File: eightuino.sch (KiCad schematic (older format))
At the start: 21 parts, among them CON1 BARREL_JACK, CON2 AVR-ISP-10, IC1 ATMEGA8-P, P1 PowerPins, P2 Analog, P3 Digital1, P4 Digital_2, SW1 SW_PUSH_SMALL, U1 NCP1117ST33T3G, X1 CRYSTAL

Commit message: Added FTDI connector in schematic
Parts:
- added C?: 100nF, symbol C
- added P?: CONN_6, symbol CONN_6
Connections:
- net +BATT: now also P?.3
- net GND: now also P?.1, P?.2
- net at CON2.5, IC1.1 (PC6(~RESET~)), P1.6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: now also C?.2
- net RX: now reaches IC1.2 ((RXD)PD0), P3.1 (P1)
- net RX: now also P?.4
- net TX: now reaches IC1.3 ((TXD)PD1), P3.2 (P2)
- net TX: now also P?.5
- new net DTR: C?.1, P?.6

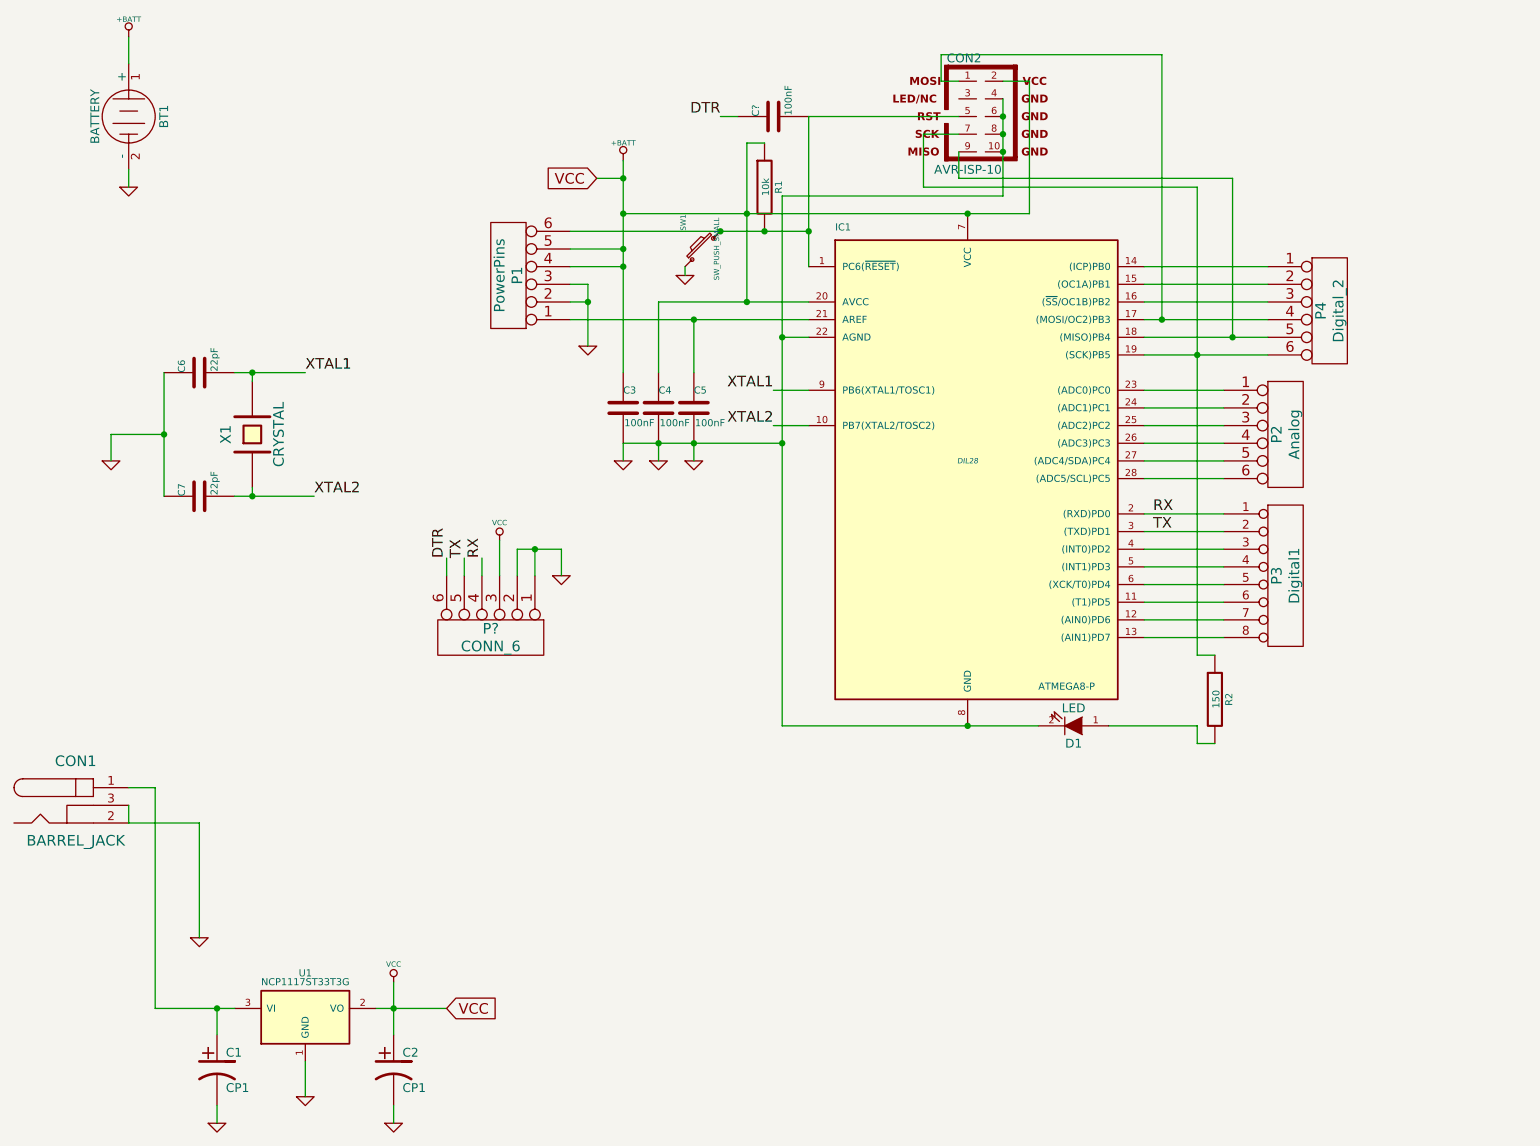
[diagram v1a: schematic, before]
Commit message: Changed schematic to 6-pin ISP
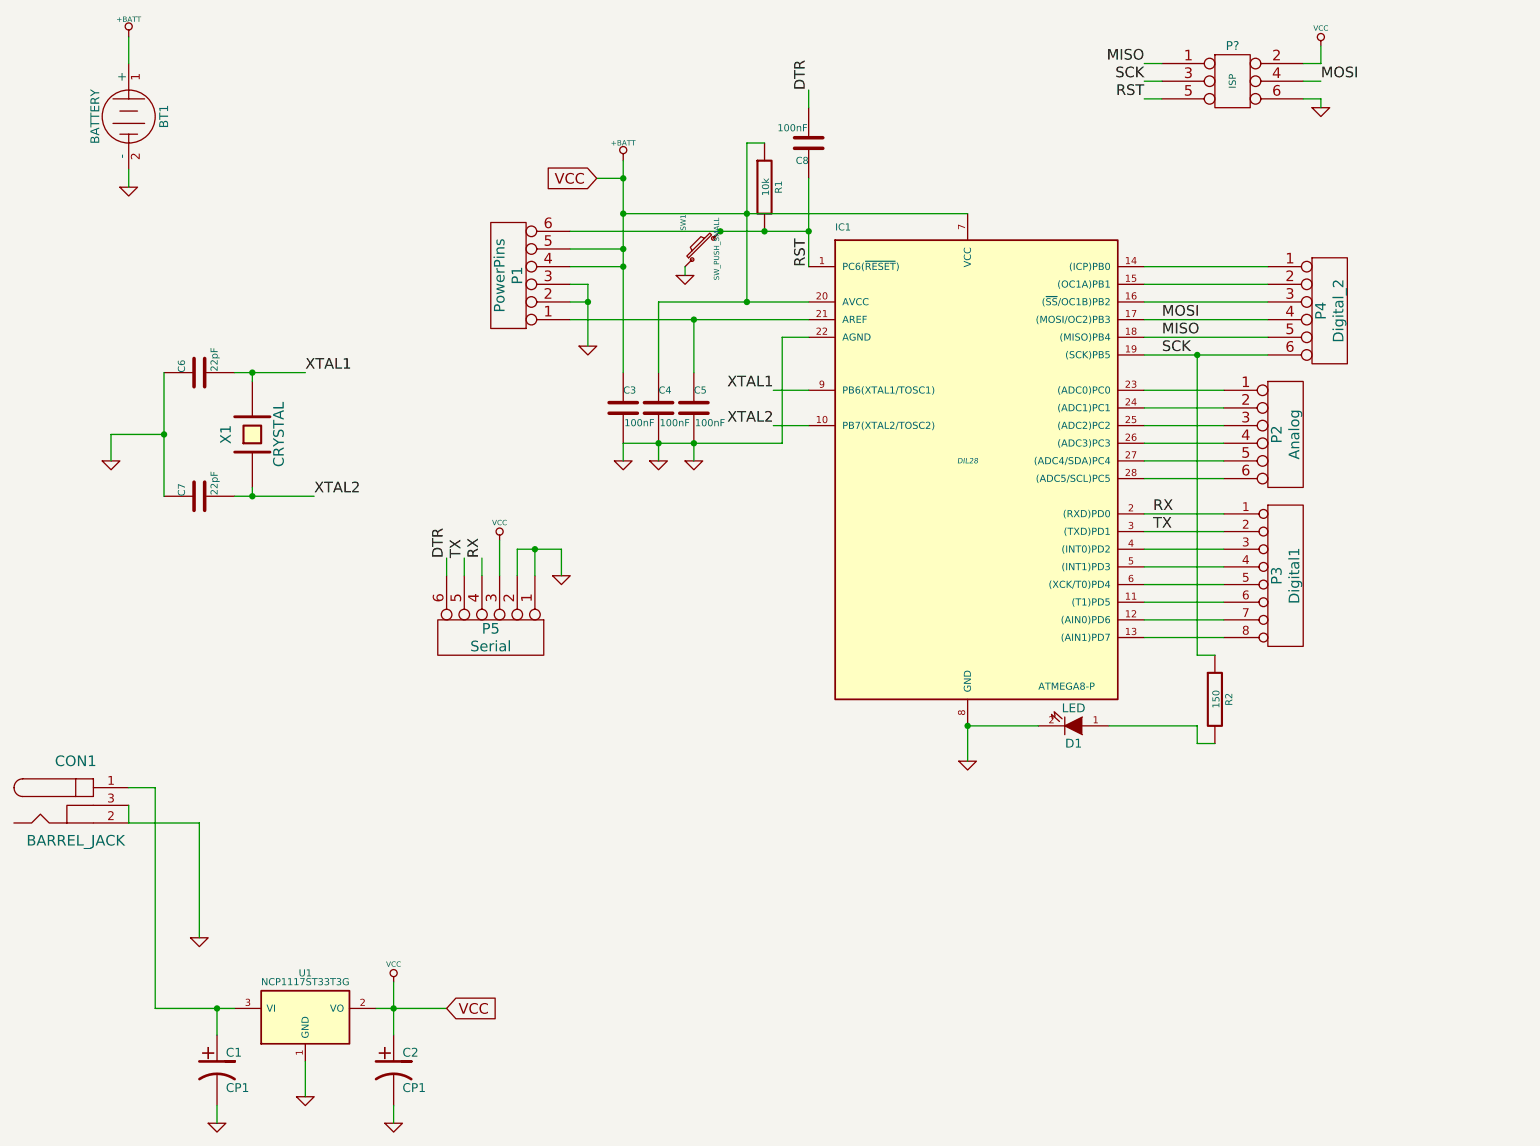
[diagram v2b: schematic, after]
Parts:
- removed CON2: AVR-ISP-10, AVR-ISP-10, symbol AVR-ISP-10
- added P?: ISP, symbol CONN_3X2
- P5: renamed from P?; value CONN_6 -> Serial
- gave numbers to parts that had none: 1
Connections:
- net +BATT: now also P?.2
- net DTR: now also C8.2; no longer C8.1
- net GND: now also P?.6
- net RST: now reaches IC1.1 (PC6(~RESET~)), P1.6, R1.2, SW1.2
- net RST: now also C8.1, P?.5; no longer C8.2
- net MOSI: now reaches IC1.17 ((MOSI/OC2)PB3), P4.4
- net MOSI: now also P?.4
- net MISO: now reaches IC1.18 ((MISO)PB4), P4.5
- net MISO: now also P?.1
- net SCK: now reaches IC1.19 ((SCK)PB5), P4.6, R2.1
- net SCK: now also P?.3
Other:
- moved on the sheet: C8

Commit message: Almost total board rework.
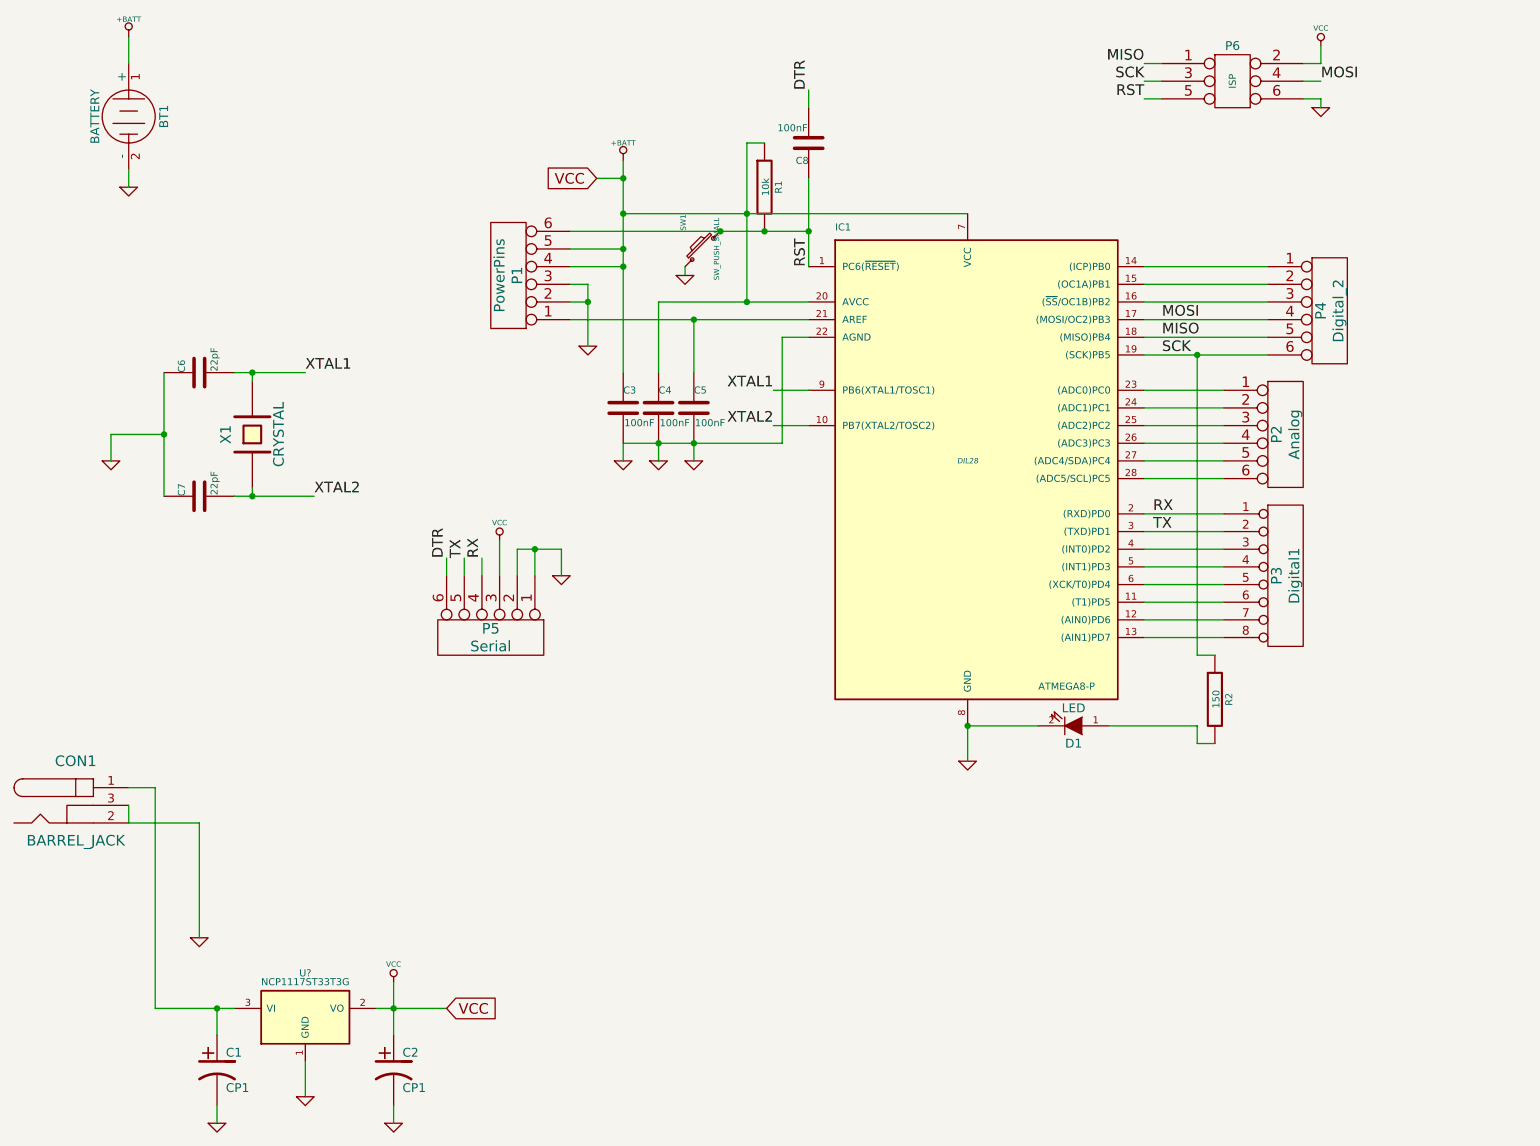
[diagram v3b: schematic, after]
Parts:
- removed U1: NCP1117ST33T3G, ~, symbol NCP1117ST33T3G
- added U?: NCP1117ST33T3G, symbol NCP1117ST33T3G
- gave numbers to parts that had none: 1
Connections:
- net +BATT: now also U?.2 (VO)
- net GND: now also U?.1 (GND)
- net at C1.1, CON1.1: now also U?.3 (VI)
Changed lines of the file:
@@
 $EndComp
 $Comp
-L GND #PWR16
+L GND #PWR01
 U 1 1 528D0B5A
 P 5300 3300
-F 0 "#PWR16" H 5300 3300 30  0001 C CNN
+F 0 "#PWR01" H 5300 3300 30  0001 C CNN
 F 1 "GND" H 5300 3230 30  0001 C CNN
 F 2 "" H 5300 3300 60  0000 C CNN
@@
 $EndComp
 $Comp
-L GND #PWR14
+L GND #PWR02
 U 1 1 528D0B67
 P 5100 3300
-F 0 "#PWR14" H 5100 3300 30  0001 C CNN
+F 0 "#PWR02" H 5100 3300 30  0001 C CNN
 F 1 "GND" H 5100 3230 30  0001 C CNN
 F 2 "" H 5100 3300 60  0000 C CNN
@@
 $EndComp
 $Comp
-L GND #PWR13
+L GND #PWR03
 U 1 1 528D0B6D
 P 4900 3300
-F 0 "#PWR13" H 4900 3300 30  0001 C CNN
+F 0 "#PWR03" H 4900 3300 30  0001 C CNN
 F 1 "GND" H 4900 3230 30  0001 C CNN
 F 2 "" H 4900 3300 60  0000 C CNN
@@
 $EndComp
 $Comp
-L GND #PWR11
+L GND #PWR04
 U 1 1 528D0D22
 P 4700 2650
-F 0 "#PWR11" H 4700 2650 30  0001 C CNN
+F 0 "#PWR04" H 4700 2650 30  0001 C CNN
 F 1 "GND" H 4700 2580 30  0001 C CNN
 F 2 "" H 4700 2650 60  0000 C CNN
@@
 $EndComp
 $Comp
-L GND #PWR15
+L GND #PWR05
 U 1 1 528D1116
 P 5250 2250
-F 0 "#PWR15" H 5250 2250 30  0001 C CNN
+F 0 "#PWR05" H 5250 2250 30  0001 C CNN
 F 1 "GND" H 5250 2180 30  0001 C CNN
 F 2 "" H 5250 2250 60  0000 C CNN
@@
 $EndComp
 $Comp
-L NCP1117ST33T3G U1
-U 1 1 5293AD98
-P 3100 6450
-F 0 "U1" H 3100 6700 40  0000 C CNN
-F 1 "NCP1117ST33T3G" H 3100 6650 40  0000 C CNN
-F 2 "~" H 3100 6450 60  0000 C CNN
-F 3 "~" H 3100 6450 60  0000 C CNN
-	1    3100 6450
-	1    0    0    -1
-$EndComp
-$Comp
-L GND #PWR4
+L GND #PWR06
 U 1 1 5293AE0F
 P 2500 6000
-F 0 "#PWR4" H 2500 6000 30  0001 C CNN
+F 0 "#PWR06" H 2500 6000 30  0001 C CNN
 F 1 "GND" H 2500 5930 30  0001 C CNN
 F 2 "" H 2500 6000 60  0000 C CNN
@@
 $EndComp
 $Comp
-L GND #PWR6
+L GND #PWR07
 U 1 1 5293AEC4
 P 3100 6900
-F 0 "#PWR6" H 3100 6900 30  0001 C CNN
+F 0 "#PWR07" H 3100 6900 30  0001 C CNN
 F 1 "GND" H 3100 6830 30  0001 C CNN
 F 2 "" H 3100 6900 60  0000 C CNN
@@
 $EndComp
 $Comp
-L GND #PWR5
+L GND #PWR08
 U 1 1 5293AF43
 P 2600 7050
-F 0 "#PWR5" H 2600 7050 30  0001 C CNN
+F 0 "#PWR08" H 2600 7050 30  0001 C CNN
 F 1 "GND" H 2600 6980 30  0001 C CNN
 F 2 "" H 2600 7050 60  0000 C CNN
@@
 $EndComp
 $Comp
-L GND #PWR8
+L GND #PWR09
 U 1 1 5293AF49
 P 3600 7050
-F 0 "#PWR8" H 3600 7050 30  0001 C CNN
+F 0 "#PWR09" H 3600 7050 30  0001 C CNN
 F 1 "GND" H 3600 6980 30  0001 C CNN
 F 2 "" H 3600 7050 60  0000 C CNN
@@
 $EndComp
 $Comp
-L GND #PWR3
+L GND #PWR010
 U 1 1 52B96E7A
 P 2100 1750
-F 0 "#PWR3" H 2100 1750 30  0001 C CNN
+F 0 "#PWR010" H 2100 1750 30  0001 C CNN
 F 1 "GND" H 2100 1680 30  0001 C CNN
 F 2 "" H 2100 1750 60  0000 C CNN
@@
 $EndComp
 $Comp
-L +BATT #PWR2
+L +BATT #PWR011
 U 1 1 52B97066
 P 2100 900
-F 0 "#PWR2" H 2100 850 20  0001 C CNN
+F 0 "#PWR011" H 2100 850 20  0001 C CNN
 F 1 "+BATT" H 2100 1000 30  0000 C CNN
 F 2 "" H 2100 900 60  0000 C CNN
@@
 $EndComp
 $Comp
-L +BATT #PWR12
+L +BATT #PWR012
 U 1 1 52B9707A
 P 4900 1600
-F 0 "#PWR12" H 4900 1550 20  0001 C CNN
+F 0 "#PWR012" H 4900 1550 20  0001 C CNN
 F 1 "+BATT" H 4900 1700 30  0000 C CNN
 F 2 "" H 4900 1600 60  0000 C CNN
@@
 $EndComp
 $Comp
-L GND #PWR1
+L GND #PWR013
 U 1 1 52B97A43
 P 2000 3300
-F 0 "#PWR1" H 2000 3300 30  0001 C CNN
+F 0 "#PWR013" H 2000 3300 30  0001 C CNN
 F 1 "GND" H 2000 3230 30  0001 C CNN
 F 2 "" H 2000 3300 60  0000 C CNN
@@
 $EndComp
 $Comp
-L GND #PWR10
+L GND #PWR014
 U 1 1 52D5A868
 P 4550 3950
-F 0 "#PWR10" H 4550 3950 30  0001 C CNN
+F 0 "#PWR014" H 4550 3950 30  0001 C CNN
 F 1 "GND" H 4550 3880 30  0001 C CNN
 F 2 "" H 4550 3950 60  0000 C CNN
@@
 $EndComp
 $Comp
-L VCC #PWR7
+L VCC #PWR015
 U 1 1 52D5AB5A
 P 3600 6250
-F 0 "#PWR7" H 3600 6350 30  0001 C CNN
+F 0 "#PWR015" H 3600 6350 30  0001 C CNN
 F 1 "VCC" H 3600 6350 30  0000 C CNN
 F 2 "" H 3600 6250 60  0000 C CNN
@@
 $EndComp
 $Comp
-L VCC #PWR9
+L VCC #PWR016
 U 1 1 52D5ACF4
 P 4200 3750
-F 0 "#PWR9" H 4200 3850 30  0001 C CNN
+F 0 "#PWR016" H 4200 3850 30  0001 C CNN
 F 1 "VCC" H 4200 3850 30  0000 C CNN
 F 2 "" H 4200 3750 60  0000 C CNN
@@
 TX
 $Comp
-L CONN_3X2 P?
+L CONN_3X2 P6
 U 1 1 52D6FAC9
 P 8350 1200
-F 0 "P?" H 8350 1450 50  0000 C CNN
+F 0 "P6" H 8350 1450 50  0000 C CNN
 F 1 "ISP" V 8350 1250 40  0000 C CNN
 F 2 "" H 8350 1200 60  0000 C CNN
@@
 MOSI
 $Comp
-L VCC #PWR?
+L VCC #PWR017
 U 1 1 52D6FB73
 P 8850 950
-F 0 "#PWR?" H 8850 1050 30  0001 C CNN
+F 0 "#PWR017" H 8850 1050 30  0001 C CNN
 F 1 "VCC" H 8850 1050 30  0000 C CNN
 F 2 "" H 8850 950 60  0000 C CNN
@@
 $EndComp
 $Comp
-L GND #PWR?
+L GND #PWR018
 U 1 1 52D6FC04
 P 8850 1300
-F 0 "#PWR?" H 8850 1300 30  0001 C CNN
+F 0 "#PWR018" H 8850 1300 30  0001 C CNN
 F 1 "GND" H 8850 1230 30  0001 C CNN
 F 2 "" H 8850 1300 60  0000 C CNN
@@
 RST
 $Comp
-L GND #PWR?
+L GND #PWR019
 U 1 1 52D7024C
 P 6850 5000
-F 0 "#PWR?" H 6850 5000 30  0001 C CNN
+F 0 "#PWR019" H 6850 5000 30  0001 C CNN
 F 1 "GND" H 6850 4930 30  0001 C CNN
 F 2 "" H 6850 5000 60  0000 C CNN
@@
 	3600 6250 3600 6550
 Wire Wire Line
-	2250 6400 2700 6400
-Wire Wire Line
 	2600 6550 2600 6400
 Wire Wire Line
@@
 Wire Wire Line
 	4900 1900 6850 1900
+Wire Wire Line
+	2250 6400 2700 6400
+$Comp
+L NCP1117ST33T3G U?
+U 1 1 52D7F944
+P 3100 6450
+F 0 "U?" H 3100 6700 40  0000 C CNN
+F 1 "NCP1117ST33T3G" H 3100 6650 40  0000 C CNN
+F 2 "" H 3100 6450 60  0000 C CNN
+F 3 "" H 3100 6450 60  0000 C CNN
+	1    3100 6450
+	1    0    0    -1
+$EndComp
 $EndSCHEMATC

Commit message: Remembered to save schematic
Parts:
- gave numbers to parts that had none: 1
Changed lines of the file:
@@
 $EndComp
 $Comp
-L GND #PWR01
+L GND #PWR16
 U 1 1 528D0B5A
 P 5300 3300
-F 0 "#PWR01" H 5300 3300 30  0001 C CNN
+F 0 "#PWR16" H 5300 3300 30  0001 C CNN
 F 1 "GND" H 5300 3230 30  0001 C CNN
 F 2 "" H 5300 3300 60  0000 C CNN
@@
 $EndComp
 $Comp
-L GND #PWR02
+L GND #PWR14
 U 1 1 528D0B67
 P 5100 3300
-F 0 "#PWR02" H 5100 3300 30  0001 C CNN
+F 0 "#PWR14" H 5100 3300 30  0001 C CNN
 F 1 "GND" H 5100 3230 30  0001 C CNN
 F 2 "" H 5100 3300 60  0000 C CNN
@@
 $EndComp
 $Comp
-L GND #PWR03
+L GND #PWR13
 U 1 1 528D0B6D
 P 4900 3300
-F 0 "#PWR03" H 4900 3300 30  0001 C CNN
+F 0 "#PWR13" H 4900 3300 30  0001 C CNN
 F 1 "GND" H 4900 3230 30  0001 C CNN
 F 2 "" H 4900 3300 60  0000 C CNN
@@
 $EndComp
 $Comp
-L GND #PWR04
+L GND #PWR11
 U 1 1 528D0D22
 P 4700 2650
-F 0 "#PWR04" H 4700 2650 30  0001 C CNN
+F 0 "#PWR11" H 4700 2650 30  0001 C CNN
 F 1 "GND" H 4700 2580 30  0001 C CNN
 F 2 "" H 4700 2650 60  0000 C CNN
@@
 $EndComp
 $Comp
-L GND #PWR05
+L GND #PWR15
 U 1 1 528D1116
 P 5250 2250
-F 0 "#PWR05" H 5250 2250 30  0001 C CNN
+F 0 "#PWR15" H 5250 2250 30  0001 C CNN
 F 1 "GND" H 5250 2180 30  0001 C CNN
 F 2 "" H 5250 2250 60  0000 C CNN
@@
 $EndComp
 $Comp
-L GND #PWR06
+L GND #PWR4
 U 1 1 5293AE0F
 P 2500 6000
-F 0 "#PWR06" H 2500 6000 30  0001 C CNN
+F 0 "#PWR4" H 2500 6000 30  0001 C CNN
 F 1 "GND" H 2500 5930 30  0001 C CNN
 F 2 "" H 2500 6000 60  0000 C CNN
@@
 $EndComp
 $Comp
-L GND #PWR07
+L GND #PWR6
 U 1 1 5293AEC4
 P 3100 6900
-F 0 "#PWR07" H 3100 6900 30  0001 C CNN
+F 0 "#PWR6" H 3100 6900 30  0001 C CNN
 F 1 "GND" H 3100 6830 30  0001 C CNN
 F 2 "" H 3100 6900 60  0000 C CNN
@@
 $EndComp
 $Comp
-L GND #PWR08
+L GND #PWR5
 U 1 1 5293AF43
 P 2600 7050
-F 0 "#PWR08" H 2600 7050 30  0001 C CNN
+F 0 "#PWR5" H 2600 7050 30  0001 C CNN
 F 1 "GND" H 2600 6980 30  0001 C CNN
 F 2 "" H 2600 7050 60  0000 C CNN
@@
 $EndComp
 $Comp
-L GND #PWR09
+L GND #PWR8
 U 1 1 5293AF49
 P 3600 7050
-F 0 "#PWR09" H 3600 7050 30  0001 C CNN
+F 0 "#PWR8" H 3600 7050 30  0001 C CNN
 F 1 "GND" H 3600 6980 30  0001 C CNN
 F 2 "" H 3600 7050 60  0000 C CNN
@@
 $EndComp
 $Comp
-L GND #PWR010
+L GND #PWR3
 U 1 1 52B96E7A
 P 2100 1750
-F 0 "#PWR010" H 2100 1750 30  0001 C CNN
+F 0 "#PWR3" H 2100 1750 30  0001 C CNN
 F 1 "GND" H 2100 1680 30  0001 C CNN
 F 2 "" H 2100 1750 60  0000 C CNN
@@
 $EndComp
 $Comp
-L +BATT #PWR011
+L +BATT #PWR2
 U 1 1 52B97066
 P 2100 900
-F 0 "#PWR011" H 2100 850 20  0001 C CNN
+F 0 "#PWR2" H 2100 850 20  0001 C CNN
 F 1 "+BATT" H 2100 1000 30  0000 C CNN
 F 2 "" H 2100 900 60  0000 C CNN
@@
 $EndComp
 $Comp
-L +BATT #PWR012
+L +BATT #PWR12
 U 1 1 52B9707A
 P 4900 1600
-F 0 "#PWR012" H 4900 1550 20  0001 C CNN
+F 0 "#PWR12" H 4900 1550 20  0001 C CNN
 F 1 "+BATT" H 4900 1700 30  0000 C CNN
 F 2 "" H 4900 1600 60  0000 C CNN
@@
 $EndComp
 $Comp
-L GND #PWR013
+L GND #PWR1
 U 1 1 52B97A43
 P 2000 3300
-F 0 "#PWR013" H 2000 3300 30  0001 C CNN
+F 0 "#PWR1" H 2000 3300 30  0001 C CNN
 F 1 "GND" H 2000 3230 30  0001 C CNN
 F 2 "" H 2000 3300 60  0000 C CNN
@@
 $EndComp
 $Comp
-L GND #PWR014
+L GND #PWR10
 U 1 1 52D5A868
 P 4550 3950
-F 0 "#PWR014" H 4550 3950 30  0001 C CNN
+F 0 "#PWR10" H 4550 3950 30  0001 C CNN
 F 1 "GND" H 4550 3880 30  0001 C CNN
 F 2 "" H 4550 3950 60  0000 C CNN
@@
 $EndComp
 $Comp
-L VCC #PWR015
+L VCC #PWR7
 U 1 1 52D5AB5A
 P 3600 6250
-F 0 "#PWR015" H 3600 6350 30  0001 C CNN
+F 0 "#PWR7" H 3600 6350 30  0001 C CNN
 F 1 "VCC" H 3600 6350 30  0000 C CNN
 F 2 "" H 3600 6250 60  0000 C CNN
@@
 $EndComp
 $Comp
-L VCC #PWR016
+L VCC #PWR9
 U 1 1 52D5ACF4
 P 4200 3750
-F 0 "#PWR016" H 4200 3850 30  0001 C CNN
+F 0 "#PWR9" H 4200 3850 30  0001 C CNN
 F 1 "VCC" H 4200 3850 30  0000 C CNN
 F 2 "" H 4200 3750 60  0000 C CNN
@@
 MOSI
 $Comp
-L VCC #PWR017
+L VCC #PWR18
 U 1 1 52D6FB73
 P 8850 950
-F 0 "#PWR017" H 8850 1050 30  0001 C CNN
+F 0 "#PWR18" H 8850 1050 30  0001 C CNN
 F 1 "VCC" H 8850 1050 30  0000 C CNN
 F 2 "" H 8850 950 60  0000 C CNN
@@
 $EndComp
 $Comp
-L GND #PWR018
+L GND #PWR19
 U 1 1 52D6FC04
 P 8850 1300
-F 0 "#PWR018" H 8850 1300 30  0001 C CNN
+F 0 "#PWR19" H 8850 1300 30  0001 C CNN
 F 1 "GND" H 8850 1230 30  0001 C CNN
 F 2 "" H 8850 1300 60  0000 C CNN
@@
 RST
 $Comp
-L GND #PWR019
+L GND #PWR17
 U 1 1 52D7024C
 P 6850 5000
-F 0 "#PWR019" H 6850 5000 30  0001 C CNN
+F 0 "#PWR17" H 6850 5000 30  0001 C CNN
 F 1 "GND" H 6850 4930 30  0001 C CNN
 F 2 "" H 6850 5000 60  0000 C CNN
@@
 	2250 6400 2700 6400
 $Comp
-L NCP1117ST33T3G U?
+L NCP1117ST33T3G U1
 U 1 1 52D7F944
 P 3100 6450
-F 0 "U?" H 3100 6700 40  0000 C CNN
+F 0 "U1" H 3100 6700 40  0000 C CNN
 F 1 "NCP1117ST33T3G" H 3100 6650 40  0000 C CNN
 F 2 "" H 3100 6450 60  0000 C CNN
